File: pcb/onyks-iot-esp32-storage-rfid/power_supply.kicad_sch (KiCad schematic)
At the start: 4 parts, among them J1 Conn_01x02_Pin, U2 TLV75733PDBV

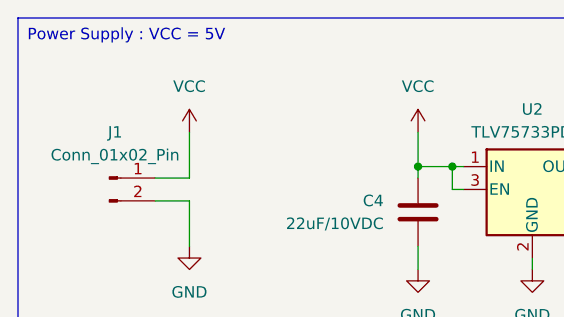
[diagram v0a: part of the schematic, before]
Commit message: oznaczenie pinów i podział elementów PCB
dodanie oznaczenia nieużywanych pinów zgodnie z opinią schematu
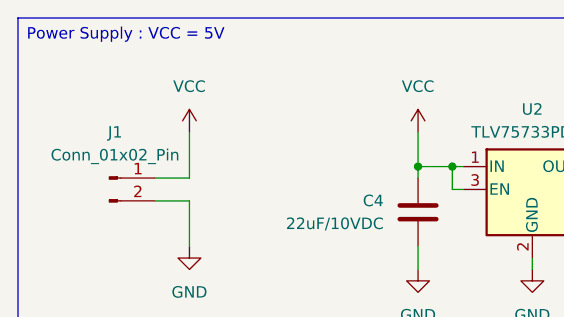
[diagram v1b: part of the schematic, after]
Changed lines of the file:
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@@
 (kicad_sch
-	(version 20231120)
+	(version 20250114)
 	(generator "eeschema")
-	(generator_version "8.0")
+	(generator_version "9.0")
 	(paper "A4")
 	(title_block
@@
 		(rev "v1.0")
 		(company "KN ONYKS")
+	)
+	(text_box "Power Supply : VCC = 5V"
+		(exclude_from_sim no)
+		(at 76.2 53.34 0)
+		(size 88.9 35.56)
+		(margins 0.9525 0.9525 0.9525 0.9525)
+		(stroke
+			(width 0)
+			(type default)
+		)
+		(fill
+			(type none)
+		)
+		(effects
+			(font
+				(size 1.27 1.27)
+			)
+			(justify left top)
+		)
 	)
 	(junction
@@
 		)
 	)
-	(text_box "Power Supply : VCC = 5V"
-		(exclude_from_sim no)
-		(at 76.2 53.34 0)
-		(size 88.9 35.56)
-		(stroke
-			(width 0)
-			(type default)
-		)
-		(fill
-			(type none)
-		)
-		(effects
-			(font
-				(size 1.27 1.27)
-			)
-			(justify left top)
-		)
-	)

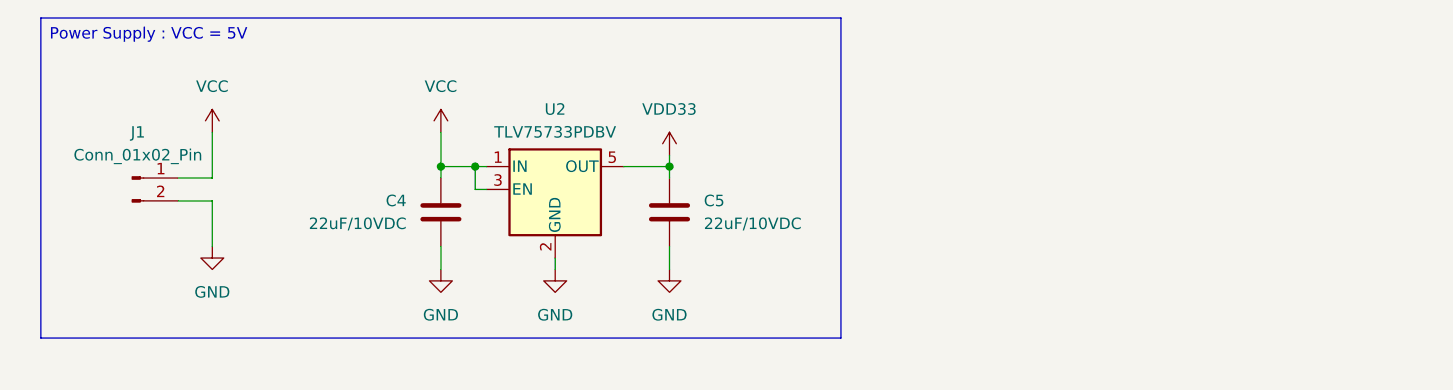
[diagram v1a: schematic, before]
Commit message: projekt PCB v2.2
Projekt gotowy do review. @przemech @Xenon02
Dodany zostal drugi stabilizator AMS1117-3.3, ktory mamy w nadmiarze w kole.
Zaktualizowano DR na zgodne z JLCPCB capabilities, ktore wczesniej byly bledne.
Dodano opis wymiarow plytki.
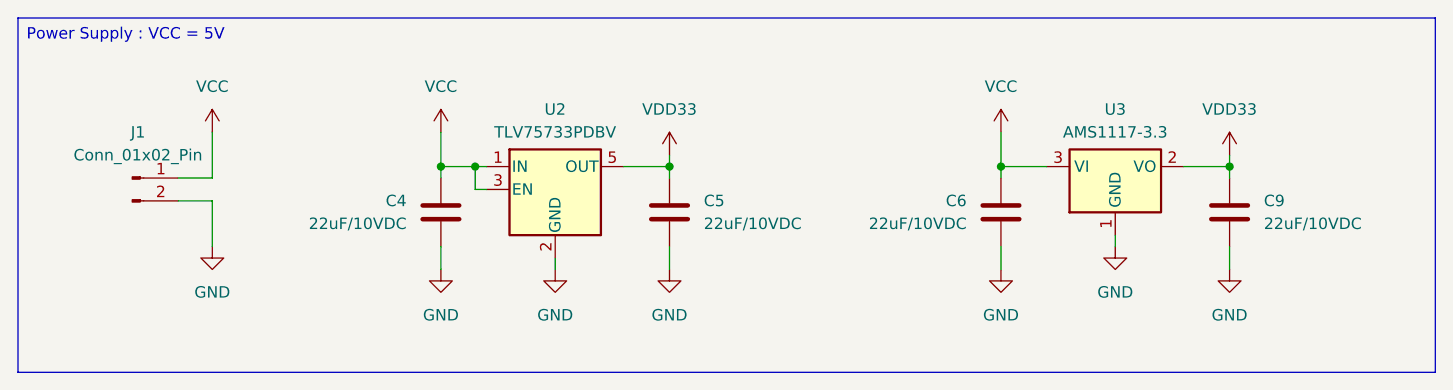
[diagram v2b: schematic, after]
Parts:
- added C6, C9: 22uF/10VDC, Capacitor_SMD:C_0603_1608Metric_Pad1.08x0.95mm_HandSolder, symbol Device:C
- added U3: AMS1117-3.3, Package_TO_SOT_SMD:SOT-223-3_TabPin2, symbol Regulator_Linear:AMS1117-3.3
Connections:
- net GND: now also C6.2, C9.2, U3.1 (GND)
- net VCC: now also C6.1, U3.3 (VI)
- net VDD33: now also C9.1, U3.2 (VO)
